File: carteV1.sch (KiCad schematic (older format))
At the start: 2 parts, among them U1 AD9954

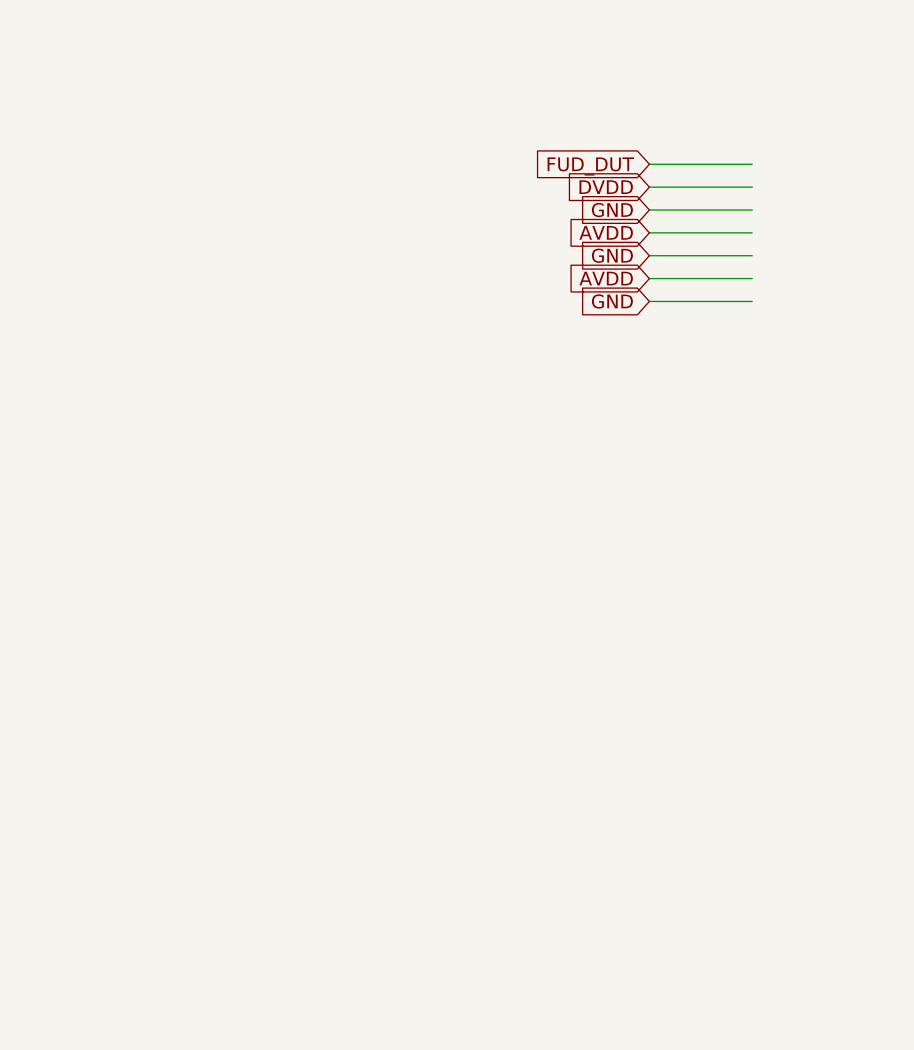
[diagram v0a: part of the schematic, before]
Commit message: Rajout de la partie XTAL
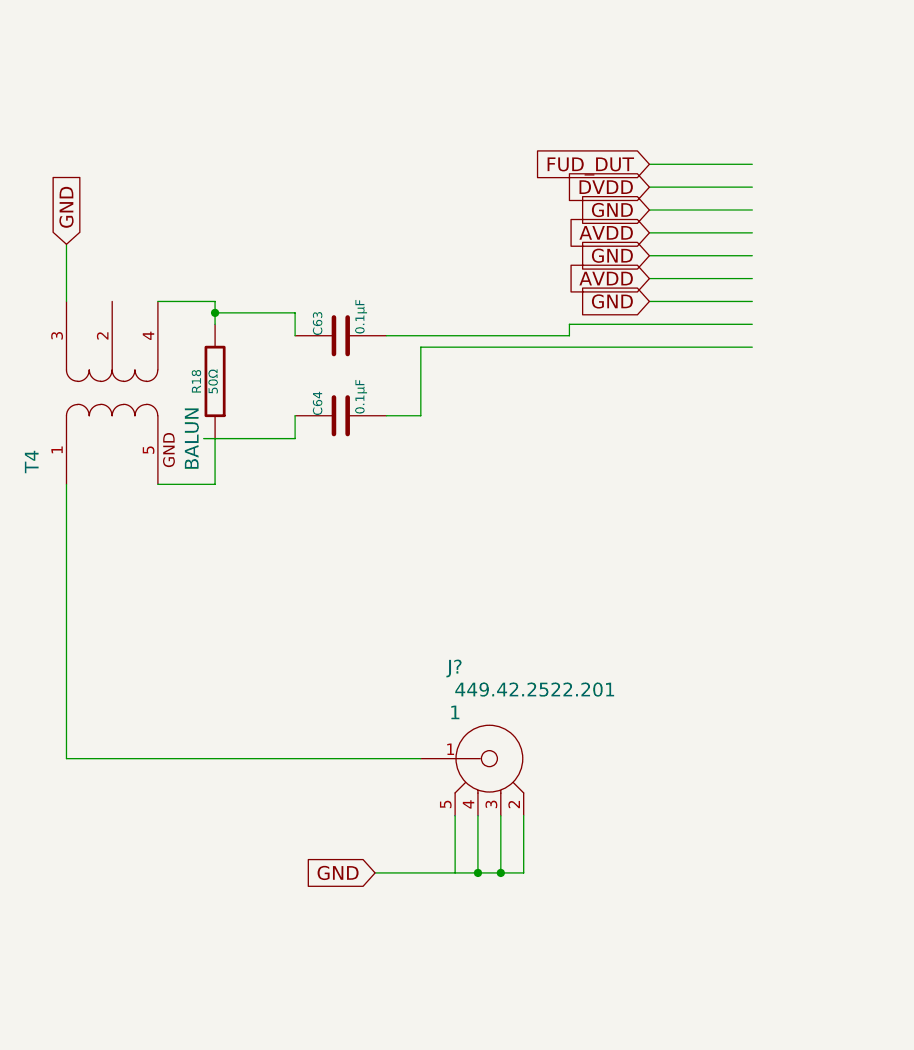
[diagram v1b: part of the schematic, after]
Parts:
- added C63, C64: 0.1μF, ~, symbol C
- added J?: 449.42.2522.201, SOLEIL-SMA-449, symbol 449.42.2522.201
- added R18: 50Ω, ~, symbol R
- added T4: BALUN, symbol BALUN
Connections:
- wire segments 8 -> 30
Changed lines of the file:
@@
 LIBS:valves
 LIBS:ad9954
+LIBS:balun
+LIBS:SMA_connectors
 LIBS:carteV1-cache
 EELAYER 27 0
@@
 Text GLabel 9300 850  0    60   Input ~ 0
 GND
+Text GLabel 3500 2700 0    60   Input ~ 0
+GND
+Text GLabel 3500 2900 0    60   Input ~ 0
+GND
+Text GLabel 3500 3100 0    60   Input ~ 0
+GND
+Text GLabel 3500 2600 0    60   Input ~ 0
+DVDD
+Text GLabel 3500 2500 0    60   Input ~ 0
+FUD_DUT
+Text GLabel 3500 2800 0    60   Input ~ 0
+AVDD
+Text GLabel 3500 3000 0    60   Input ~ 0
+AVDD
+$Comp
+L BALUN T4
+U 1 1 53791146
+P 1150 3500
+F 0 "T4" H 850 3850 60  0000 C CNN
+F 1 "BALUN" H 950 3150 60  0000 C CNN
+F 2 "" H 1150 3500 60  0000 C CNN
+F 3 "" H 1150 3500 60  0000 C CNN
+	1    1150 3500
+	0    -1   -1   0
+$EndComp
+Text GLabel 950  2850 1    60   Input ~ 0
+GND
+$Comp
+L 449.42.2522.201 J?
+U 1 1 537912AE
+P 2500 5100
+F 0 "J?" H 2650 5500 60  0000 C CNN
+F 1 "449.42.2522.201" H 3000 5400 60  0000 C CNN
+F 2 "SOLEIL-SMA-449" H 3450 5250 60  0001 C CNN
+F 3 "" H 2500 5100 60  0000 C CNN
+F 4 "IMS" H 3150 5150 60  0001 C CNN "Manufacturer"
+F 5 "449.42.2522.201" H 3450 5050 60  0001 C CNN "Manufacturer ref"
+F 6 "PN Electronics" H 3400 4950 60  0001 C CNN "Supplier"
+F 7 "449.42.2522.201" H 3450 4850 60  0001 C CNN "Supplier ref"
+F 8 "1" H 2650 5300 60  0000 C CNN "Qty"
+F 9 "-" H 3100 4750 60  0001 C CNN "Desc1"
+F 10 "-" H 3100 4650 60  0001 C CNN "Desc2"
+F 11 "-" H 3100 4550 60  0001 C CNN "Desc3"
+F 12 "-" H 3200 4550 60  0001 C CNN "Desc4"
+F 13 "IMS 449" H 3250 4450 60  0001 C CNN "Case"
+F 14 "58" H 3100 4350 60  0001 C CNN "Price"
+	1    2500 5100
+	1    0    0    -1
+$EndComp
+Text GLabel 2300 5600 0    60   Input ~ 0
+GND
+$Comp
+L R R18
+U 1 1 537913D8
+P 1600 3450
+F 0 "R18" V 1680 3450 40  0000 C CNN
+F 1 "50Ω" V 1607 3451 40  0000 C CNN
+F 2 "~" V 1530 3450 30  0000 C CNN
+F 3 "~" H 1600 3450 30  0000 C CNN
+	1    1600 3450
+	-1   0    0    1
+$EndComp
 Wire Wire Line
 	9300 850  9600 850
-Text GLabel 3500 2700 0    60   Input ~ 0
-GND
 Wire Wire Line
 	3500 2700 3950 2700
-Text GLabel 3500 2900 0    60   Input ~ 0
-GND
 Wire Wire Line
 	3500 2900 3950 2900
-Text GLabel 3500 3100 0    60   Input ~ 0
-GND
 Wire Wire Line
 	3500 3100 3950 3100
-Text GLabel 3500 2600 0    60   Input ~ 0
-DVDD
 Wire Wire Line
 	3500 2600 3950 2600
-Text GLabel 3500 2500 0    60   Input ~ 0
-FUD_DUT
 Wire Wire Line
 	3500 2500 3950 2500
-Text GLabel 3500 2800 0    60   Input ~ 0
-AVDD
 Wire Wire Line
 	3500 2800 3950 2800
-Text GLabel 3500 3000 0    60   Input ~ 0
-AVDD
 Wire Wire Line
 	3500 3000 3950 3000
+Wire Wire Line
+	2300 5600 2950 5600
+Wire Wire Line
+	2650 5350 2650 5600
+Wire Wire Line
+	2750 5600 2750 5350
+Wire Wire Line
+	2850 5600 2850 5350
+Connection ~ 2750 5600
+Wire Wire Line
+	2950 5600 2950 5350
+Connection ~ 2850 5600
+Wire Wire Line
+	950  3900 950  5100
+Wire Wire Line
+	950  5100 2500 5100
+Wire Wire Line
+	950  3100 950  2850
+$Comp
+L C C64
+U 1 1 537914B2
+P 2150 3600
+F 0 "C64" H 2150 3700 40  0000 L CNN
+F 1 "0.1μF" H 2156 3515 40  0000 L CNN
+F 2 "~" H 2188 3450 30  0000 C CNN
+F 3 "~" H 2150 3600 60  0000 C CNN
+	1    2150 3600
+	0    -1   -1   0
+$EndComp
+$Comp
+L C C63
+U 1 1 537914C1
+P 2150 3250
+F 0 "C63" H 2150 3350 40  0000 L CNN
+F 1 "0.1μF" H 2156 3165 40  0000 L CNN
+F 2 "~" H 2188 3100 30  0000 C CNN
+F 3 "~" H 2150 3250 60  0000 C CNN
+	1    2150 3250
+	0    -1   -1   0
+$EndComp
+Wire Wire Line
+	1350 3100 1600 3100
+Wire Wire Line
+	1600 3100 1600 3200
+Wire Wire Line
+	1350 3900 1600 3900
+Wire Wire Line
+	1600 3900 1600 3700
+Wire Wire Line
+	1550 3700 1950 3700
+Wire Wire Line
+	1950 3700 1950 3600
+Wire Wire Line
+	1600 3150 1950 3150
+Wire Wire Line
+	1950 3150 1950 3250
+Connection ~ 1600 3150
+Wire Wire Line
+	2350 3250 3150 3250
+Wire Wire Line
+	3150 3250 3150 3200
+Wire Wire Line
+	3150 3200 3950 3200
+Wire Wire Line
+	2350 3600 2500 3600
+Wire Wire Line
+	2500 3600 2500 3300
+Wire Wire Line
+	2500 3300 3950 3300
 $EndSCHEMATC

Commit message: Filtre
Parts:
- added C61: 0.01μF, ~, symbol C
- added C? (x7): C, ~, symbol C
- added J12: FILTER_IOUT_DUT2, SOLEIL-SMA-449, symbol 449.42.2522.201
- added J7: CRYSTAL OUTDUT2, SOLEIL-SMA-449, symbol 449.42.2522.201
- added L? (x3): INDUCTOR_SMALL, ~, symbol INDUCTOR_SMALL
- added R16: 243Ω, ~, symbol R
- J6: renamed from J?; value 449.42.2522.201 -> REF_CLK_DUT2
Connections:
- net labels added: CLKMODESEL_DUT2, XTAL_AUTO
- wire segments 30 -> 61

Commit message: Filtre
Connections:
- wire segments 61 -> 63
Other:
- moved on the sheet: C61, R16
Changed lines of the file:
@@
 Sheet 1 1
 Title "AD9954 - GENERATION SIGNAL HF"
-Date "18 may 2014"
+Date "19 may 2014"
 Rev "0.1"
 Comp "Polytech'Tours"
@@
 Text GLabel 3500 3500 0    60   Input ~ 0
 CLKMODESEL_DUT2
-Text GLabel 1700 4200 0    60   Input ~ 0
+Text GLabel 2300 4550 0    60   Input ~ 0
 AVDD
 $Comp
 L C C61
 U 1 1 53791846
-P 2350 4200
-F 0 "C61" H 2350 4300 40  0000 L CNN
-F 1 "0.01μF" H 2356 4115 40  0000 L CNN
-F 2 "~" H 2388 4050 30  0000 C CNN
-F 3 "~" H 2350 4200 60  0000 C CNN
-	1    2350 4200
+P 2950 4550
+F 0 "C61" H 2950 4650 40  0000 L CNN
+F 1 "0.01μF" H 2956 4465 40  0000 L CNN
+F 2 "~" H 2988 4400 30  0000 C CNN
+F 3 "~" H 2950 4550 60  0000 C CNN
+	1    2950 4550
 	0    -1   -1   0
 $EndComp
@@
 L R R16
 U 1 1 53791855
-P 3100 4200
-F 0 "R16" V 3180 4200 40  0000 C CNN
-F 1 "243Ω" V 3107 4201 40  0000 C CNN
-F 2 "~" V 3030 4200 30  0000 C CNN
-F 3 "~" H 3100 4200 30  0000 C CNN
-	1    3100 4200
+P 3700 4550
+F 0 "R16" V 3780 4550 40  0000 C CNN
+F 1 "243Ω" V 3707 4551 40  0000 C CNN
+F 2 "~" V 3630 4550 30  0000 C CNN
+F 3 "~" H 3700 4550 30  0000 C CNN
+	1    3700 4550
 	0    -1   -1   0
 $EndComp
@@
 	1    0    0    -1
 $EndComp
-Wire Wire Line
-	9300 850  9600 850
-Wire Wire Line
-	3500 2700 3950 2700
-Wire Wire Line
-	3500 2900 3950 2900
-Wire Wire Line
-	3500 3100 3950 3100
-Wire Wire Line
-	3500 2600 3950 2600
-Wire Wire Line
-	3500 2500 3950 2500
-Wire Wire Line
-	3500 2800 3950 2800
-Wire Wire Line
-	3500 3000 3950 3000
-Wire Wire Line
-	2300 5600 2950 5600
-Wire Wire Line
-	2650 5350 2650 5600
-Wire Wire Line
-	2750 5600 2750 5350
-Wire Wire Line
-	2850 5600 2850 5350
-Connection ~ 2750 5600
-Wire Wire Line
-	2950 5600 2950 5350
-Connection ~ 2850 5600
-Wire Wire Line
-	950  3900 950  5100
-Wire Wire Line
-	950  5100 2500 5100
-Wire Wire Line
-	950  3100 950  2850
-Wire Wire Line
-	1350 3100 1600 3100
-Wire Wire Line
-	1600 3100 1600 3200
-Wire Wire Line
-	1350 3900 1600 3900
-Wire Wire Line
-	1600 3900 1600 3700
-Wire Wire Line
-	1550 3700 1950 3700
-Wire Wire Line
-	1950 3700 1950 3600
-Wire Wire Line
-	1600 3150 1950 3150
-Wire Wire Line
-	1950 3150 1950 3250
-Connection ~ 1600 3150
-Wire Wire Line
-	2350 3250 3150 3250
-Wire Wire Line
-	3150 3250 3150 3200
-Wire Wire Line
-	3150 3200 3950 3200
-Wire Wire Line
-	2350 3600 2500 3600
-Wire Wire Line
-	2500 3600 2500 3300
-Wire Wire Line
-	2500 3300 3950 3300
-Wire Wire Line
-	3500 3400 3950 3400
-Wire Wire Line
-	3500 3500 3950 3500
-Wire Wire Line
-	1700 4200 2150 4200
-Wire Wire Line
-	2550 4200 2850 4200
-Wire Wire Line
-	3350 4200 3350 3600
-Wire Wire Line
-	3350 3600 3950 3600
-Wire Wire Line
-	4000 5600 4650 5600
-Wire Wire Line
-	4350 5350 4350 5600
-Wire Wire Line
-	4450 5600 4450 5350
-Wire Wire Line
-	4550 5600 4550 5350
-Connection ~ 4450 5600
-Wire Wire Line
-	4650 5600 4650 5350
-Connection ~ 4550 5600
-Wire Wire Line
-	3750 5100 4200 5100
-Wire Wire Line
-	2150 6900 2800 6900
-Wire Wire Line
-	2500 6650 2500 6900
-Wire Wire Line
-	2600 6900 2600 6650
-Wire Wire Line
-	2700 6900 2700 6650
-Connection ~ 2600 6900
-Connection ~ 2700 6900
-Wire Wire Line
-	2800 6900 2800 6650
-Wire Wire Line
-	3350 7450 5300 7450
-Connection ~ 4050 7450
-Wire Wire Line
-	4050 7600 4050 7450
-Wire Wire Line
-	4050 6450 4050 7050
-Wire Wire Line
-	4000 6900 4150 6900
-Connection ~ 4050 6900
-Wire Wire Line
-	4650 6900 4800 6900
-Wire Wire Line
-	4700 6450 4700 7050
-Connection ~ 4700 6900
-Wire Wire Line
-	4550 6450 4800 6450
-Connection ~ 4700 6450
-Wire Wire Line
-	4000 6450 4150 6450
-Connection ~ 4050 6450
-Wire Wire Line
-	3350 7050 3350 6900
-Wire Wire Line
-	3350 6900 3500 6900
-Wire Wire Line
-	3500 6900 3500 6450
-Wire Wire Line
-	3500 6450 3600 6450
-Wire Wire Line
-	5300 6450 5300 7050
-Wire Wire Line
-	5300 6450 5200 6450
 $Comp
 L C C?
@@
 	1    0    0    -1
 $EndComp
+Text GLabel 2900 2800 1    60   Input ~ 0
+GND
+Text GLabel 2550 3750 3    60   Input ~ 0
+GND
+Wire Wire Line
+	9300 850  9600 850
+Wire Wire Line
+	3500 2700 3950 2700
+Wire Wire Line
+	3500 2900 3950 2900
+Wire Wire Line
+	3500 3100 3950 3100
+Wire Wire Line
+	3500 2600 3950 2600
+Wire Wire Line
+	3500 2500 3950 2500
+Wire Wire Line
+	3500 2800 3950 2800
+Wire Wire Line
+	3500 3000 3950 3000
+Wire Wire Line
+	2300 5600 2950 5600
+Wire Wire Line
+	2650 5350 2650 5600
+Wire Wire Line
+	2750 5600 2750 5350
+Wire Wire Line
+	2850 5600 2850 5350
+Connection ~ 2750 5600
+Wire Wire Line
+	2950 5600 2950 5350
+Connection ~ 2850 5600
+Wire Wire Line
+	950  3900 950  5100
+Wire Wire Line
+	950  5100 2500 5100
+Wire Wire Line
+	950  3100 950  2850
+Wire Wire Line
+	1350 3100 1600 3100
+Wire Wire Line
+	1600 3100 1600 3200
+Wire Wire Line
+	1350 3900 1600 3900
+Wire Wire Line
+	1600 3900 1600 3700
+Wire Wire Line
+	1550 3700 1950 3700
+Wire Wire Line
+	1950 3700 1950 3600
+Wire Wire Line
+	1600 3150 1950 3150
+Wire Wire Line
+	1950 3150 1950 3250
+Connection ~ 1600 3150
+Wire Wire Line
+	2350 3250 3150 3250
+Wire Wire Line
+	3150 3250 3150 3200
+Wire Wire Line
+	3150 3200 3950 3200
+Wire Wire Line
+	2350 3600 2500 3600
+Wire Wire Line
+	2500 3600 2500 3300
+Wire Wire Line
+	2500 3300 3950 3300
+Wire Wire Line
+	3500 3400 3950 3400
+Wire Wire Line
+	3500 3500 3950 3500
+Wire Wire Line
+	2300 4550 2750 4550
+Wire Wire Line
+	3150 4550 3450 4550
+Wire Wire Line
+	3950 3600 3950 4550
+Wire Wire Line
+	4000 5600 4650 5600
+Wire Wire Line
+	4350 5350 4350 5600
+Wire Wire Line
+	4450 5600 4450 5350
+Wire Wire Line
+	4550 5600 4550 5350
+Connection ~ 4450 5600
+Wire Wire Line
+	4650 5600 4650 5350
+Connection ~ 4550 5600
+Wire Wire Line
+	3750 5100 4200 5100
+Wire Wire Line
+	2150 6900 2800 6900
+Wire Wire Line
+	2500 6650 2500 6900
+Wire Wire Line
+	2600 6900 2600 6650
+Wire Wire Line
+	2700 6900 2700 6650
+Connection ~ 2600 6900
+Connection ~ 2700 6900
+Wire Wire Line
+	2800 6900 2800 6650
+Wire Wire Line
+	3350 7450 4700 7450
+Connection ~ 4050 7450
+Wire Wire Line
+	4050 7600 4050 7450
+Wire Wire Line
+	4050 6450 4050 7050
+Wire Wire Line
+	4000 6900 4150 6900
+Connection ~ 4050 6900
+Wire Wire Line
+	4650 6900 4800 6900
+Wire Wire Line
+	4700 6450 4700 7050
+Connection ~ 4700 6900
+Wire Wire Line
+	4550 6450 4800 6450
+Connection ~ 4700 6450
+Wire Wire Line
+	4000 6450 4150 6450
+Connection ~ 4050 6450
+Wire Wire Line
+	3350 7050 3350 6900
+Wire Wire Line
+	3350 6900 3500 6900
+Wire Wire Line
+	3500 6900 3500 6450
+Wire Wire Line
+	3500 6450 3600 6450
+Wire Wire Line
+	5300 6450 5300 7050
+Wire Wire Line
+	5300 6450 5200 6450
 Connection ~ 5300 6900
-Connection ~ 4700 7450
+Wire Wire Line
+	2900 2800 2900 3250
+Wire Wire Line
+	2550 3750 2550 3300
+Wire Wire Line
+	4699 7450 5300 7450
+Connection ~ 4699 7450
+Connection ~ 5300 7450
+Connection ~ 3350 7450
+Connection ~ 3500 6900
+Connection ~ 3600 6450
+Connection ~ 4000 6450
+Connection ~ 4150 6450
+Connection ~ 4550 6450
+Connection ~ 4800 6450
+Connection ~ 5200 6450
+Connection ~ 4150 6900
+Connection ~ 4650 6900
+Connection ~ 4800 6900
+Connection ~ 3350 7050
+Connection ~ 4050 7050
+Connection ~ 4700 7050
+Connection ~ 5300 7050
 $EndSCHEMATC

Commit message: Avancement
- Ajout de la lib MAX.. SPI/USB
- Ajout d’un connecteur MINI USB
-Ajout d’un convertisseur CC … plus qu’a le câblé
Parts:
- added C35, C36: 18pF, ~, symbol C
- added CON?: USB-MINI-B, symbol USB-MINI-B
- added DA?: LP2981, symbol LP2981
- added IC?: MAX3421E-1, TQFP32-5MM, symbol MAX3421E-1
- added X1: 25mhz, ~, symbol CRYSTAL
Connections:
- wire segments 63 -> 71
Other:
- moved on the sheet: C63, U1
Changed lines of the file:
@@
 LIBS:SMA_connectors
 LIBS:inductor
+LIBS:oscillator-cmos-out-4
+LIBS:MAX3421E-1-259960
+LIBS:Power_kl
 LIBS:carteV1-cache
 EELAYER 27 0
@@
 L AD9954 U1
 U 1 1 5378E4A6
-P 9000 5800
-F 0 "U1" H 5550 8500 60  0000 C CNN
-F 1 "AD9954" H 5550 8700 159 0000 C CNN
-F 2 "~" H 5550 8700 60  0000 C CNN
-F 3 "~" H 5550 8700 60  0000 C CNN
-	1    9000 5800
+P 8400 5250
+F 0 "U1" H 4950 7950 60  0000 C CNN
+F 1 "AD9954" H 4950 8150 159 0000 C CNN
+F 2 "~" H 4950 8150 60  0000 C CNN
+F 3 "~" H 4950 8150 60  0000 C CNN
+	1    8400 5250
 	1    0    0    -1
 $EndComp
@@
 L C C63
 U 1 1 537914C1
-P 2150 3250
-F 0 "C63" H 2150 3350 40  0000 L CNN
-F 1 "0.1μF" H 2156 3165 40  0000 L CNN
-F 2 "~" H 2188 3100 30  0000 C CNN
-F 3 "~" H 2150 3250 60  0000 C CNN
-	1    2150 3250
-	0    -1   -1   0
-$EndComp
-Text GLabel 3500 3400 0    60   Input ~ 0
+P 2150 3000
+F 0 "C63" H 2150 3100 40  0000 L CNN
+F 1 "0.1μF" H 2156 2915 40  0000 L CNN
+F 2 "~" H 2188 2850 30  0000 C CNN
+F 3 "~" H 2150 3000 60  0000 C CNN
+	1    2150 3000
+	0    -1   -1   0
+$EndComp
+Text GLabel 2350 4200 0    60   Input ~ 0
 XTAL_AUTO
-Text GLabel 3500 3500 0    60   Input ~ 0
+Text GLabel 2350 4300 0    60   Input ~ 0
 CLKMODESEL_DUT2
 Text GLabel 2300 4550 0    60   Input ~ 0
@@
 	1    0    0    -1
 $EndComp
-Text GLabel 2900 2800 1    60   Input ~ 0
-GND
-Text GLabel 2550 3750 3    60   Input ~ 0
-GND
+Text GLabel 2200 2600 0    60   Input ~ 0
+GND
+Text GLabel 2250 4000 0    60   Input ~ 0
+GND
+$Comp
+L CRYSTAL X1
+U 1 1 537A0ADF
+P 2340 3300
+F 0 "X1" H 2340 3450 60  0000 C CNN
+F 1 "25mhz" H 2340 3150 60  0000 C CNN
+F 2 "~" H 2340 3300 60  0000 C CNN
+F 3 "ECS-250-18-4X-DU" V 2850 4077 60  0000 C CNN
+	1    2340 3300
+	0    -1   -1   0
+$EndComp
+$Comp
+L C C36
+U 1 1 537A0D25
+P 2350 2800
+F 0 "C36" H 2350 2900 40  0000 L CNN
+F 1 "18pF" H 2356 2715 40  0000 L CNN
+F 2 "~" H 2388 2650 30  0000 C CNN
+F 3 "" H 2350 2800 60  0000 C CNN
+	1    2350 2800
+	-1   0    0    1
+$EndComp
+$Comp
+L C C35
+U 1 1 537A0D2B
+P 2350 3800
+F 0 "C35" H 2350 3900 40  0000 L CNN
+F 1 "18pF" H 2356 3715 40  0000 L CNN
+F 2 "~" H 2388 3650 30  0000 C CNN
+F 3 "~" H 2350 3800 60  0000 C CNN
+	1    2350 3800
+	-1   0    0    1
+$EndComp
 Wire Wire Line
 	9300 850  9600 850
@@
 Wire Wire Line
 	1950 3700 1950 3600
-Wire Wire Line
-	1600 3150 1950 3150
-Wire Wire Line
-	1950 3150 1950 3250
 Connection ~ 1600 3150
-Wire Wire Line
-	2350 3250 3150 3250
-Wire Wire Line
-	3150 3250 3150 3200
-Wire Wire Line
-	3150 3200 3950 3200
-Wire Wire Line
-	2350 3600 2500 3600
-Wire Wire Line
-	2500 3600 2500 3300
-Wire Wire Line
-	2500 3300 3950 3300
-Wire Wire Line
-	3500 3400 3950 3400
-Wire Wire Line
-	3500 3500 3950 3500
 Wire Wire Line
 	2300 4550 2750 4550
@@
 	5300 6450 5200 6450
 Connection ~ 5300 6900
-Wire Wire Line
-	2900 2800 2900 3250
-Wire Wire Line
-	2550 3750 2550 3300
 Wire Wire Line
 	4699 7450 5300 7450
@@
 Connection ~ 4700 7050
 Connection ~ 5300 7050
+Connection ~ 2350 3000
+Connection ~ 2350 3600
+Connection ~ 1950 3600
+Wire Wire Line
+	1586 3142 1948 3142
+Wire Wire Line
+	1948 3142 1948 3000
+Wire Wire Line
+	1948 3000 1952 3000
+Wire Wire Line
+	3936 3192 3936 3213
+Wire Wire Line
+	3936 3213 2589 3213
+Wire Wire Line
+	2589 3213 2589 2991
+Wire Wire Line
+	2589 2991 2337 2991
+Wire Wire Line
+	2346 3603 2616 3603
+Wire Wire Line
+	2616 3603 2616 3294
+Wire Wire Line
+	2616 3294 3948 3294
+Wire Wire Line
+	2346 4209 2694 4209
+Wire Wire Line
+	2694 4209 2694 3393
+Wire Wire Line
+	2694 3393 3945 3393
+Wire Wire Line
+	2337 4293 2784 4293
+Wire Wire Line
+	2784 4293 2784 3501
+Wire Wire Line
+	2784 3501 3942 3501
+Wire Wire Line
+	2244 4002 2346 4002
+Wire Wire Line
+	2346 4002 2346 3999
+Wire Wire Line
+	2190 2598 2340 2598
+Wire Wire Line
+	2340 2598 2340 2595
+Connection ~ 2200 2600
+Connection ~ 2350 2600
+Connection ~ 2250 4000
+Connection ~ 2350 4000
+$Comp
+L USB-MINI-B CON?
+U 1 1 537A55F1
+P 10363 5968
+F 0 "CON?" H 10113 6418 60  0000 C CNN
+F 1 "USB-MINI-B" H 10313 5468 60  0000 C CNN
+F 2 "" H 10363 5968 60  0000 C CNN
+F 3 "" H 10363 5968 60  0000 C CNN
+	1    10363 5968
+	1    0    0    -1
+$EndComp
+$Comp
+L LP2981 DA?
+U 1 1 537A68F4
+P 9718 4566
+F 0 "DA?" H 9568 4866 60  0000 C CNN
+F 1 "LP2981" H 9718 4766 60  0000 C CNN
+F 2 "" H 9718 4566 60  0000 C CNN
+F 3 "" H 9718 4566 60  0000 C CNN
+	1    9718 4566
+	1    0    0    -1
+$EndComp
+$Comp
+L MAX3421E-1 IC?
+U 1 1 537A7593
+P 8548 5832
+F 0 "IC?" H 7948 6382 50  0000 L BNN
+F 1 "MAX3421E-1" H 8295 5836 50  0000 L BNN
+F 2 "TQFP32-5MM" H 8548 5982 50  0001 C CNN
+F 3 "" H 8548 5832 60  0000 C CNN
+	1    8548 5832
+	1    0    0    -1
+$EndComp
 $EndSCHEMATC

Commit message: Modification : Alimentation & USB
-Ajout des 2 alimentations + ref
-Modification du MAX
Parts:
- removed DA?: LP2981, symbol LP2981
- removed U1: AD9954, ~, symbol AD9954
- added C? (x6): 10uF, ~, symbol CAPAPOL
- added C? (x2): 20pF, ~, symbol C
- added U? (x2): LM1117MP-3.3, symbol LM1117MP-3.3
- added U?: AD9954, ~, symbol AD9954
- added X?: 16mhz, ~, symbol CRYSTAL
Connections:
- net labels added: 1V8, 3V3, 5V, D+, D-
- wire segments 71 -> 144
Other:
- moved on the sheet: IC?, P?

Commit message: Update
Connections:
- wire segments 144 -> 169
